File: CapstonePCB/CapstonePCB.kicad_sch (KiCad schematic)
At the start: 18 parts, among them J1 Conn_02x40_Counter_Clockwise, J2 Barrel_Jack, U1 NUCLEO64-F411RE, U2 LP-MSPM0G3507, U3 STSPIN220

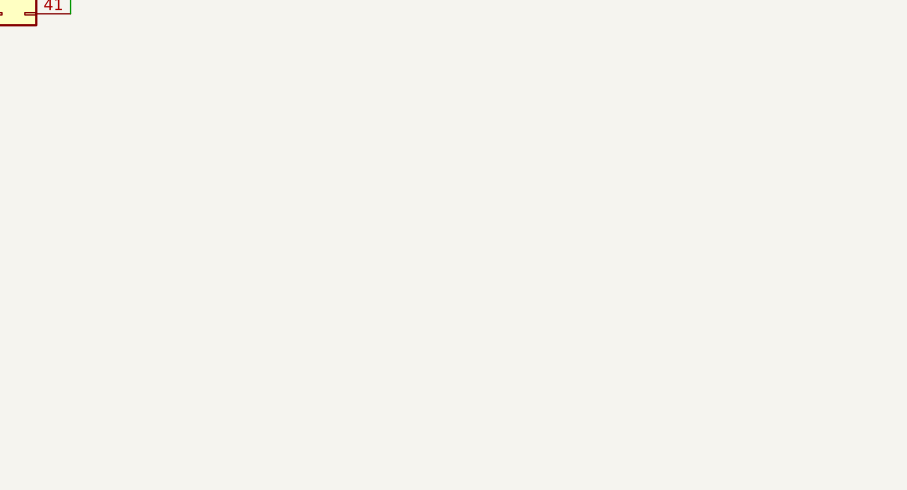
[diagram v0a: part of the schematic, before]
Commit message: Added RC filter + schmitt trigger
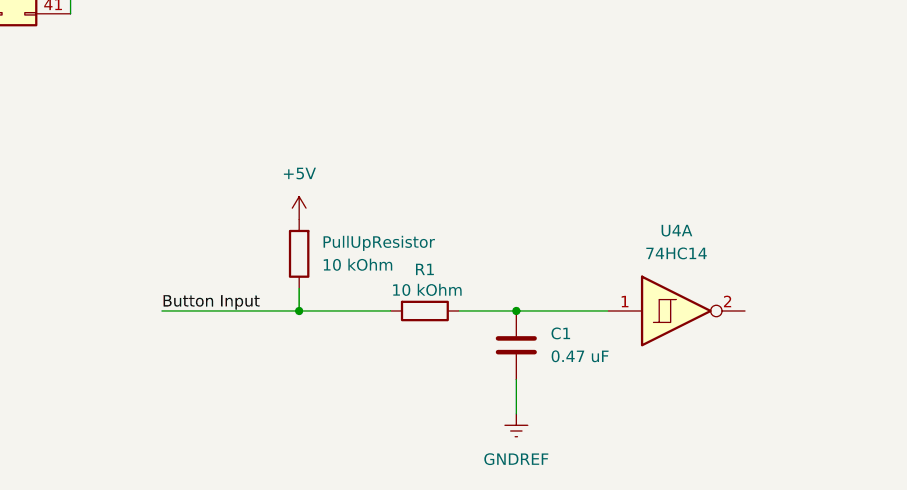
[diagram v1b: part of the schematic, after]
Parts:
- added C1: 0.47 uF, symbol Device:C
- added PullUpResistor, R1: 10 kOhm, symbol Device:R
- added U4: 74HC14, symbol 74xx:74HC14
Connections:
- net +5V: now also PullUpResistor.2
- net GNDREF: now also C1.2
- new net: C1.1, R1.1, U4.1
- new net Button Input: PullUpResistor.1, R1.2

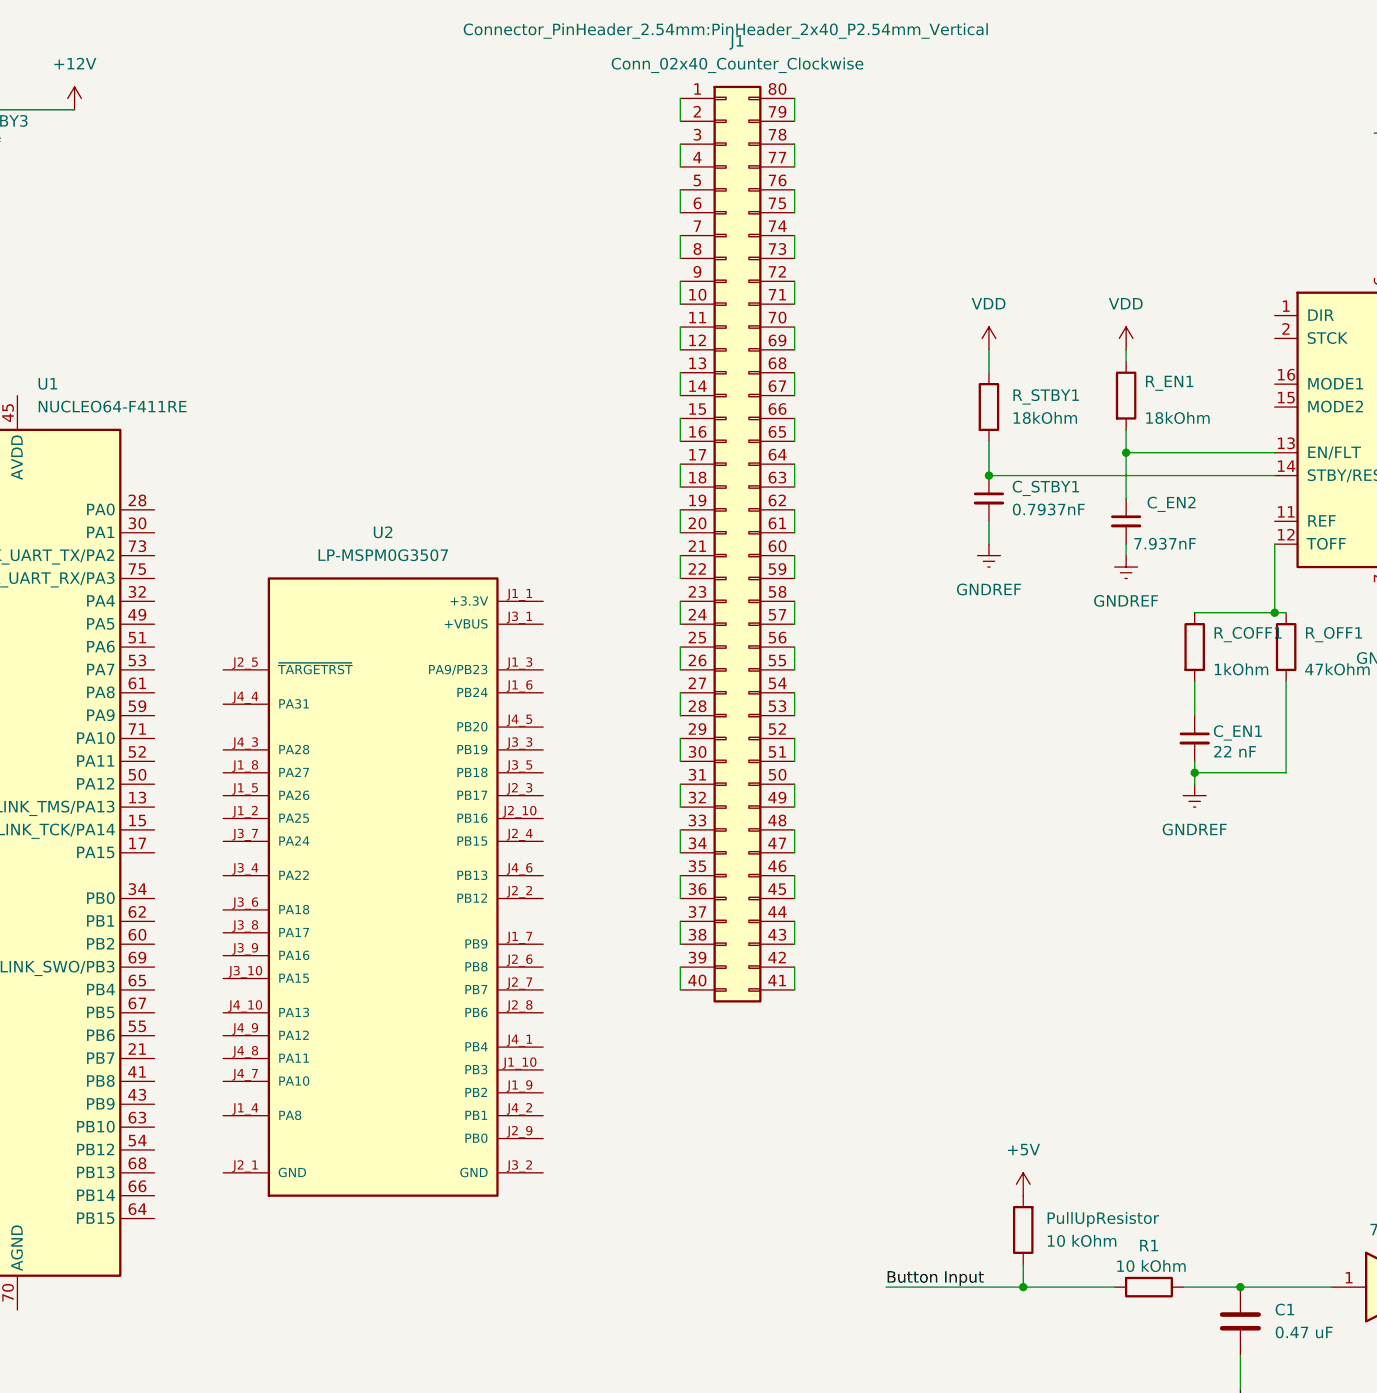
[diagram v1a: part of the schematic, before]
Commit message: Added LDOs for 5v and 3.3v rails
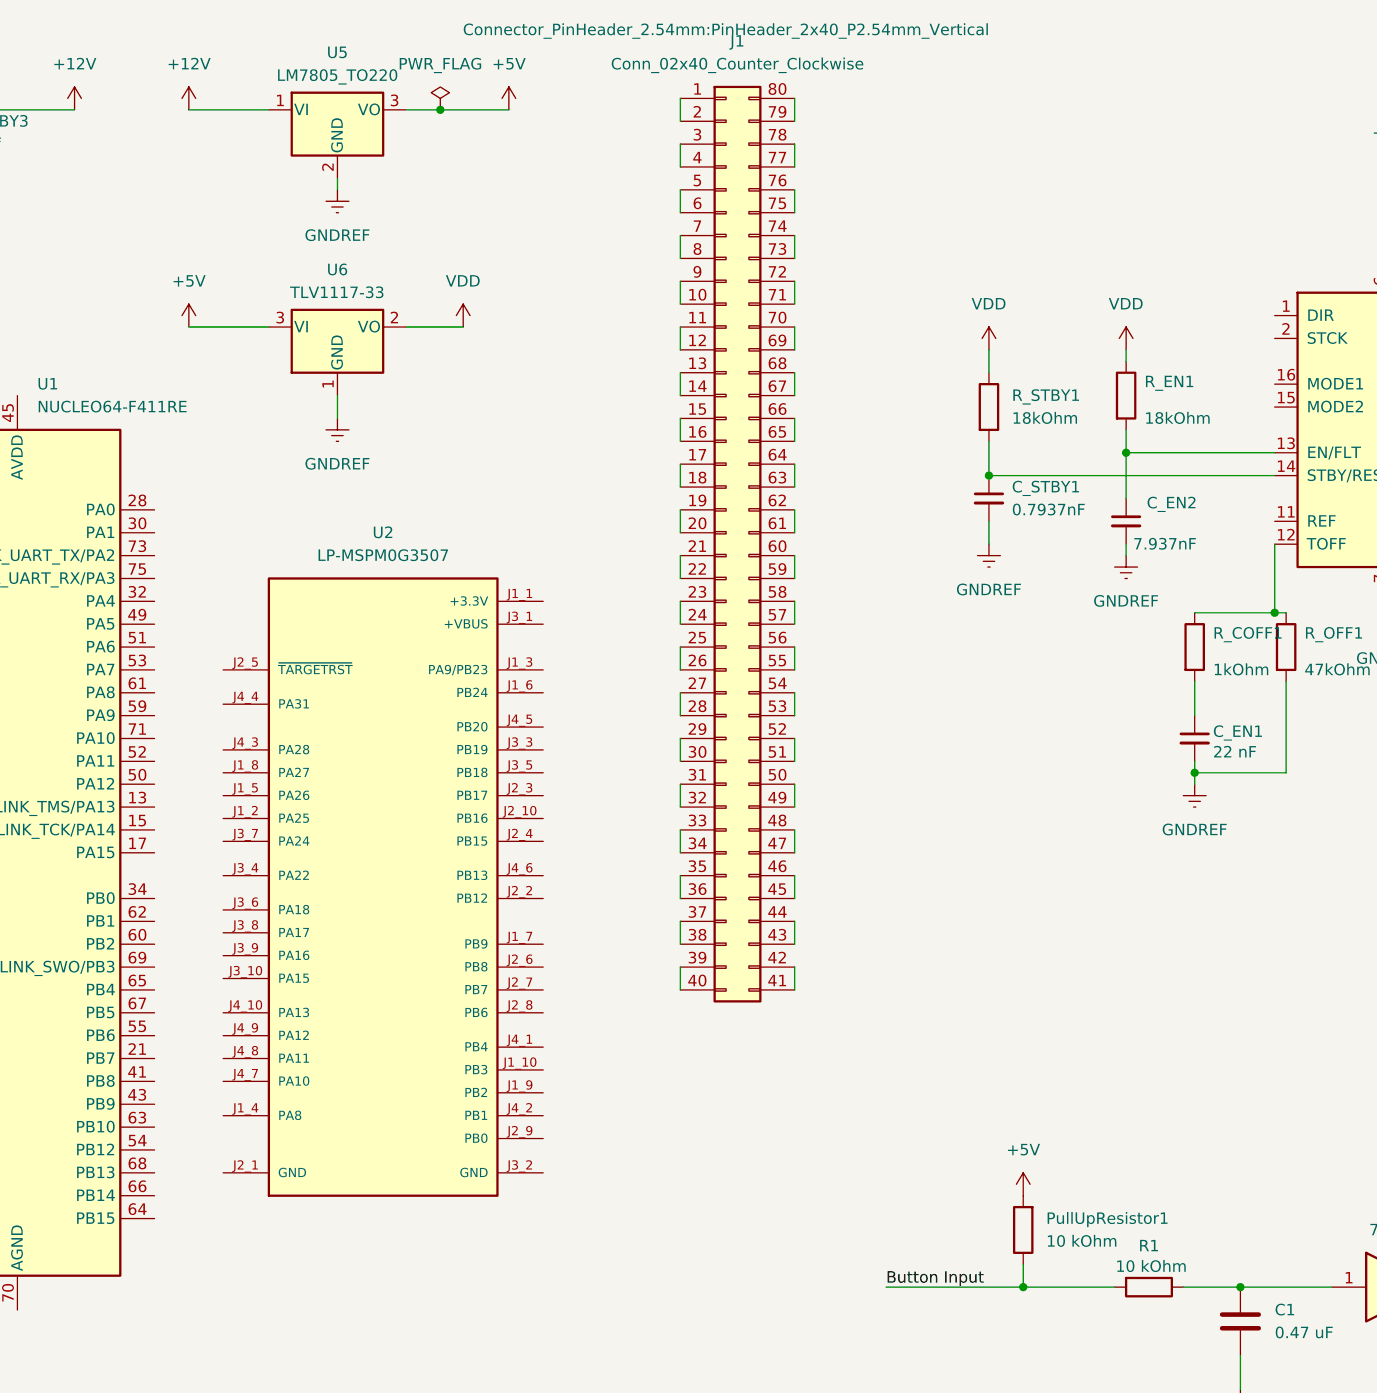
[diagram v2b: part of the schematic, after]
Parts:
- added U5: LM7805_TO220, Package_TO_SOT_THT:TO-220-3_Vertical, symbol Regulator_Linear:LM7805_TO220
- added U6: TLV1117-33, Package_TO_SOT_SMD:SOT-223-3_TabPin2, symbol Regulator_Linear:TLV1117-33
- renumbered PullUpResistor to PullUpResistor1
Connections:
- net +12V: now also U5.1 (VI)
- net +5V: now also U5.3 (VO), U6.3 (VI)
- net GNDREF: now also U5.2 (GND), U6.1 (GND)
- net VDD: now also U6.2 (VO)

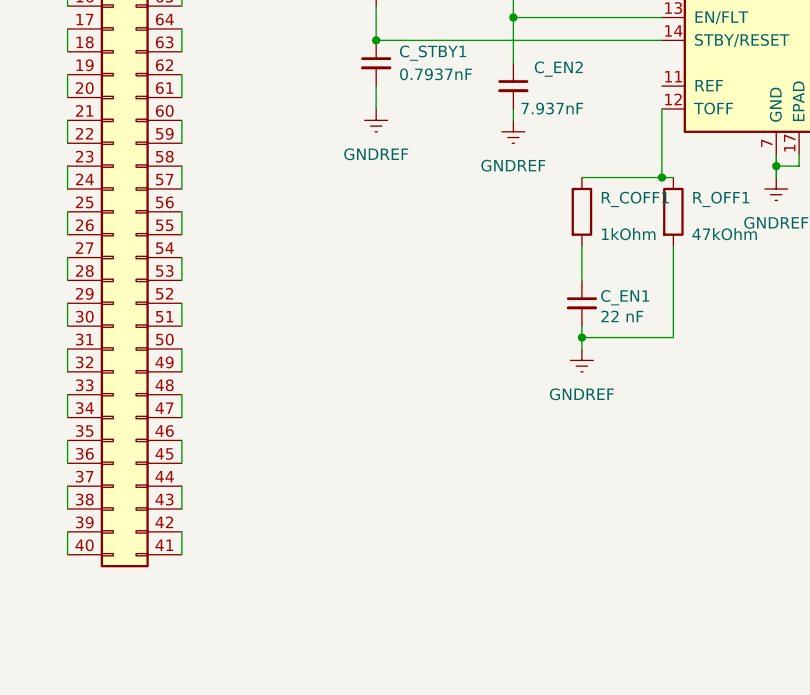
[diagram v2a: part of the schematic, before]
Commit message: Added RGB led to schematic
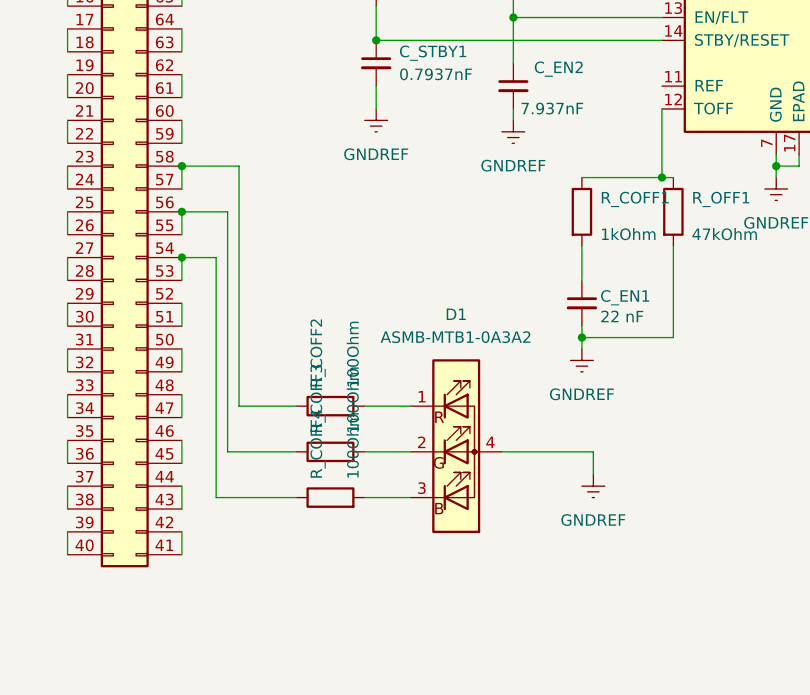
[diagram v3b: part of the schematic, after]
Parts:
- added D1: ASMB-MTB1-0A3A2, LED_SMD:LED_Avago_PLCC4_3.2x2.8mm_CW, symbol LED:ASMB-MTB1-0A3A2
- added R_COFF2, R_COFF3, R_COFF4: 100Ohm, Resistor_SMD:R_0201_0603Metric, symbol Device:R
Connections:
- net GNDREF: now also D1.4 (A)
- net at J1.53 (Pin_53), J1.54 (Pin_54): now also R_COFF4.1
- net at J1.55 (Pin_55), J1.56 (Pin_56): now also R_COFF3.1
- net at J1.57 (Pin_57), J1.58 (Pin_58): now also R_COFF2.1
- new net: D1.2 (GK), R_COFF3.2
- new net: D1.1 (RK), R_COFF2.2
- new net: D1.3 (BK), R_COFF4.2

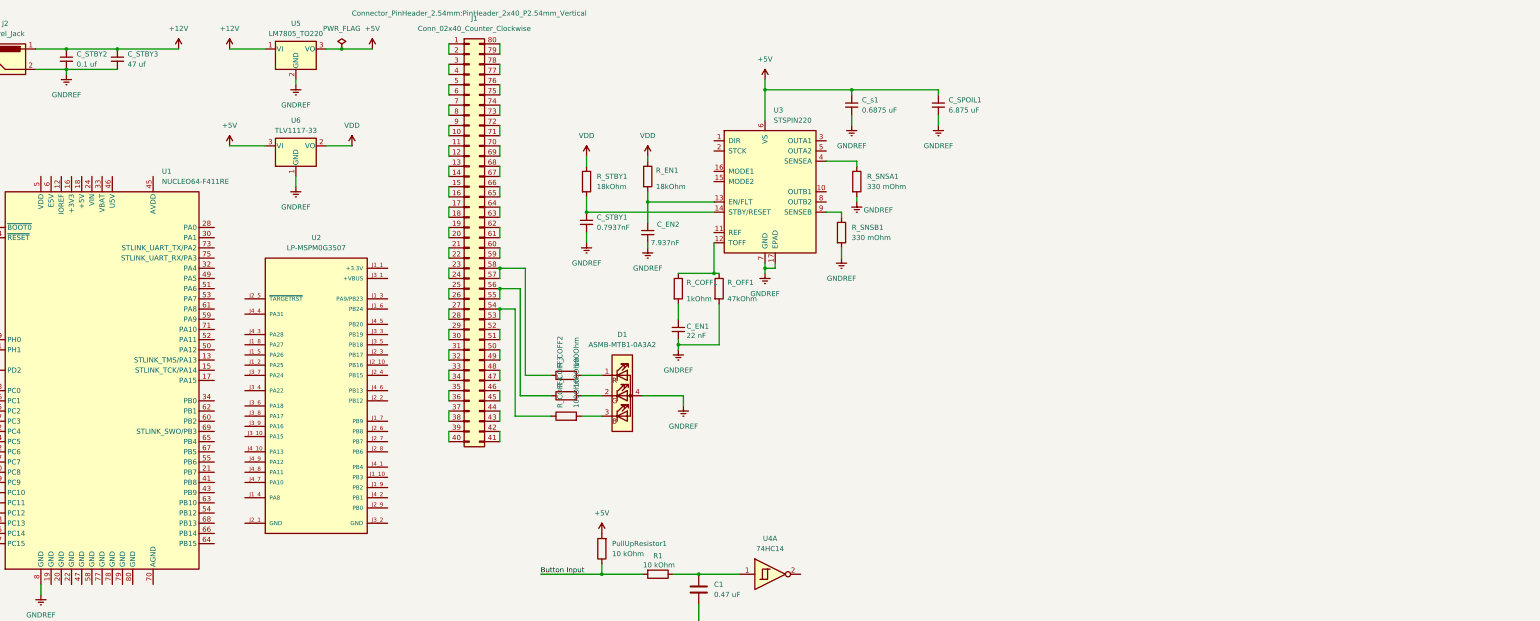
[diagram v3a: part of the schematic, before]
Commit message: Added I2C light sensor to schematic
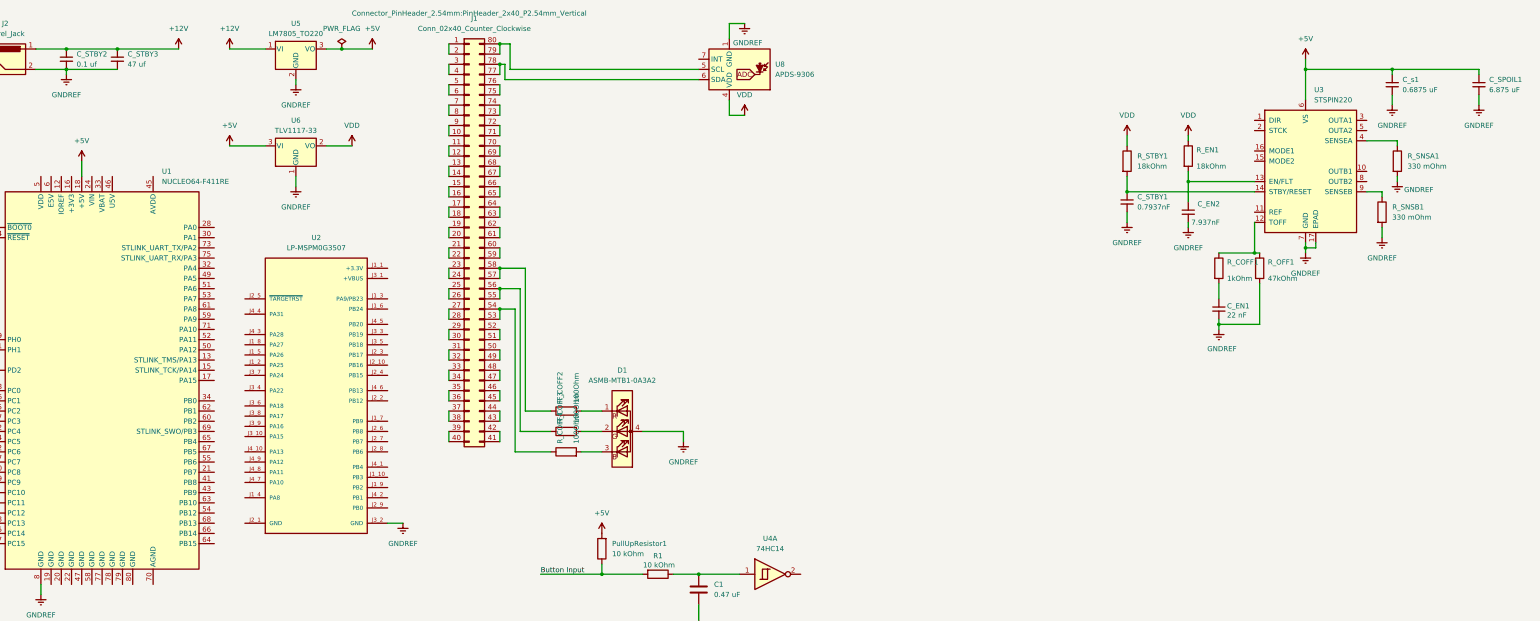
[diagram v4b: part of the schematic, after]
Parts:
- added U8: APDS-9306, OptoDevice:Broadcom_LGA-8_2x2mm_P0.53mm, symbol Sensor_Optical:APDS-9306
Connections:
- net +5V: now also U1.18 (+5V)
- net GNDREF: now also U2.J3_2 (GND), U8.1 (GND)
- net VDD: now also U8.4 (VDD)
- net at J1.77 (Pin_77), J1.78 (Pin_78): now also U8.6 (SDA)
- net at J1.79 (Pin_79), J1.80 (Pin_80): now also U8.5 (SCL)
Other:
- moved on the sheet: C_EN1, C_EN2, C_SPOIL1, C_STBY1, C_s1, D1, R_COFF1, R_COFF2, R_COFF3, R_COFF4, R_EN1, R_OFF1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
